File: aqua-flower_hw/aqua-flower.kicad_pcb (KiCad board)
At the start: 2 copper layers, 0 parts

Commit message: Place all pcb details and start to trace pcb.
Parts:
- added BZ1: BUZZER, Buzzers_Beepers:Buzzer_12x9.5RM7.6, F.Cu at (125.6, 93.8)
- added C1: 0.1u, Capacitors_SMD:C_0603_HandSoldering, F.Cu at (134.2, 99.0)
- added C10: 4u7, Capacitors_SMD:C_0603_HandSoldering, F.Cu at (180.8, 78.1)
- added C11: 0.1u, Capacitors_SMD:C_0603_HandSoldering, F.Cu at (184.7, 72.0)
- added C2: 4u7, Capacitors_SMD:C_0603_HandSoldering, F.Cu at (175.3, 92.2)
- added C3: 0.1u, Capacitors_SMD:C_0603_HandSoldering, F.Cu at (165.2, 100.3)
- added C4: 0.1u, Capacitors_SMD:C_0603_HandSoldering, F.Cu at (185.0, 77.9)
- added C5: 0.1u, Capacitors_SMD:C_0603_HandSoldering, F.Cu at (169.6, 94.4)
- added C6: 0.1u, Capacitors_SMD:C_0603_HandSoldering, F.Cu at (180.8, 84.0)
- added C7: 1u, Capacitors_SMD:C_0603_HandSoldering, F.Cu at (161.0, 100.3)
- added C8: 8p, Capacitors_SMD:C_0603_HandSoldering, F.Cu at (175.3, 86.3)
- added C9: 8p, Capacitors_SMD:C_0603_HandSoldering, F.Cu at (165.5, 94.4)
- added DA1: LD1117, TO_SOT_Packages_SMD:SOT-223, F.Cu at (150.6, 89.9)
- added DD1: STM32F100C8(B), Housings_QFP:LQFP-48_7x7mm_Pitch0.5mm, F.Cu at (144.7, 78.0)
- added Q1: NPN, TO_SOT_Packages_SMD:SOT-23_Handsoldering, F.Cu at (162.8, 70.3)
- added Q2: IRLML6302, TO_SOT_Packages_SMD:SOT-23_Handsoldering, F.Cu at (178.0, 62.1)
- added Q3: IRLML6302, TO_SOT_Packages_SMD:SOT-23_Handsoldering, F.Cu at (155.6, 75.9)
- added Q4: IRLML6302, TO_SOT_Packages_SMD:SOT-23_Handsoldering, F.Cu at (168.9, 70.3)
- added Q5: IRLML6302, TO_SOT_Packages_SMD:SOT-23_Handsoldering, F.Cu at (140.8, 98.2)
- added R1: 1k, Resistors_SMD:R_0603_HandSoldering, F.Cu at (156.7, 100.3)
- added R2: 10k, Resistors_SMD:R_0603_HandSoldering, F.Cu at (161.2, 94.4)
- added R3: 10k, Resistors_SMD:R_0603_HandSoldering, F.Cu at (156.7, 94.4)
- added R4: 10k, Resistors_SMD:R_0603_HandSoldering, F.Cu at (184.8, 66.1)
- added R5: 10k, Resistors_SMD:R_0603_HandSoldering, F.Cu at (184.5, 60.2)
- added SW1: BUTTON, Buttons_Switches_ThroughHole:SW_PUSH_SMALL, F.Cu at (177.9, 71.0)
- added SW2: BUTTON, Buttons_Switches_ThroughHole:SW_PUSH_SMALL, F.Cu at (168.5, 87.3)
- added SW3: BUTTON, Buttons_Switches_ThroughHole:SW_PUSH_SMALL, F.Cu at (174.0, 79.2)
- added SW4: BUTTON, Buttons_Switches_ThroughHole:SW_PUSH_SMALL, F.Cu at (149.8, 98.8)
- added SW5: BUTTON, Buttons_Switches_ThroughHole:SW_PUSH_SMALL, F.Cu at (159.1, 87.3)
- added SW6: BUTTON, Buttons_Switches_ThroughHole:SW_PUSH_SMALL, F.Cu at (164.6, 79.2)
- added XL1: CONN_5, Socket_Strips:Socket_Strip_Straight_1x05, F.Cu at (103.5, 99.1)
- added XL2: CONN_8, Socket_Strips:Socket_Strip_Straight_1x08, F.Cu at (103.5, 63.4)
- added XL3: CONN_3, Socket_Strips:Socket_Strip_Straight_1x03, F.Cu at (139.7, 91.2)
- added XL4: ST_SWD, Socket_Strips:Socket_Strip_Straight_1x04, F.Cu at (164.0, 63.4)
- added XL5: CONN_3, Connect:BARREL_JACK, F.Cu at (149.9, 64.3)
- added XL6: CONN_3, Connect:BARREL_JACK, F.Cu at (126.9, 78.0)
- added XL7: CONN_3, Connect:BARREL_JACK, F.Cu at (108.1, 86.2)
- added XL8: CONN_3, Connect:BARREL_JACK, F.Cu at (131.1, 64.3)
- added XL9: CONN_3, Connect:BARREL_JACK, F.Cu at (108.1, 72.5)
- added XTAL1: CRYSTAL, Crystals:Crystal_Watch, F.Cu at (134.3, 85.5)

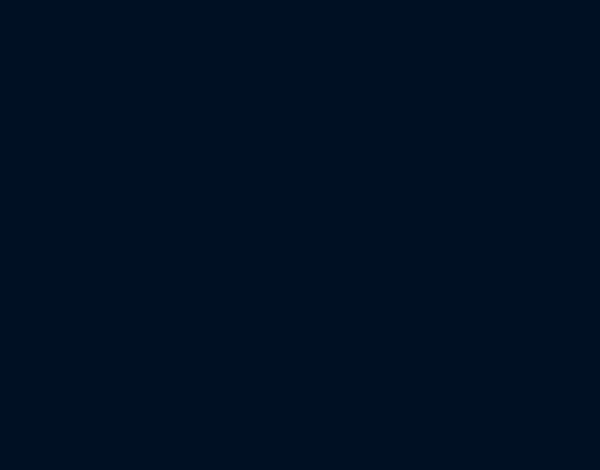
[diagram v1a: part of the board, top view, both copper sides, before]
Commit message: Reset Library Component
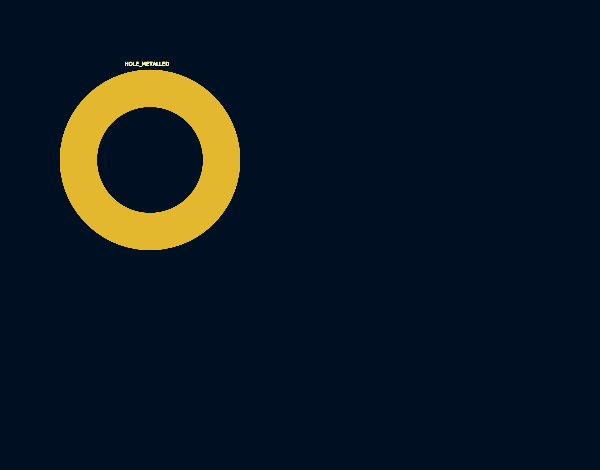
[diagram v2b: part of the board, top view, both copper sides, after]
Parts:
- added HOLE1, HOLE2, HOLE3, HOLE4: HOLE_METALLED, PCB:Hole3_5_out6mm, F.Cu at (0.00, 0.00)
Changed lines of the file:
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@@
 (kicad_pcb (version 4) (host pcbnew 4.0.2-stable)
   (general
-    (links 110)
-    (no_connects 110)
+    (links 114)
+    (no_connects 111)
     (area 0 0 0 0)
     (thickness 1.5)
@@
     (tracks 0)
     (zones 0)
-    (modules 40)
+    (modules 44)
     (nets 53)
   )
@@
       (net 52 "Net-(XL9-Pad3)"))
   )
+  (module PCB:Hole3_5_out6mm (layer F.Cu)
+    (at 0 0)
+    (fp_text reference HOLE1 (at 0 3.2004) (layer F.SilkS) hide
+      (effects (font (size 0.127 0.127) (thickness 0.00254)))
+    )
+    (fp_text value HOLE_METALLED (at -0.09906 -3.2004) (layer F.SilkS)
+      (effects (font (size 0.127 0.127) (thickness 0.00254)))
+    )
+    (pad H thru_hole circle (at 0 0) (size 6 6) (drill 3.5) (layers *.Cu *.Mask F.SilkS)
+      (net 2 GND))
+  )
+  (module PCB:Hole3_5_out6mm (layer F.Cu)
+    (at 0 0)
+    (fp_text reference HOLE2 (at 0 3.2004) (layer F.SilkS) hide
+      (effects (font (size 0.127 0.127) (thickness 0.00254)))
+    )
+    (fp_text value HOLE_METALLED (at -0.09906 -3.2004) (layer F.SilkS)
+      (effects (font (size 0.127 0.127) (thickness 0.00254)))
+    )
+    (pad H thru_hole circle (at 0 0) (size 6 6) (drill 3.5) (layers *.Cu *.Mask F.SilkS)
+      (net 2 GND))
+  )
+  (module PCB:Hole3_5_out6mm (layer F.Cu)
+    (at 0 0)
+    (fp_text reference HOLE3 (at 0 3.2004) (layer F.SilkS) hide
+      (effects (font (size 0.127 0.127) (thickness 0.00254)))
+    )
+    (fp_text value HOLE_METALLED (at -0.09906 -3.2004) (layer F.SilkS)
+      (effects (font (size 0.127 0.127) (thickness 0.00254)))
+    )
+    (pad H thru_hole circle (at 0 0) (size 6 6) (drill 3.5) (layers *.Cu *.Mask F.SilkS)
+      (net 2 GND))
+  )
+  (module PCB:Hole3_5_out6mm (layer F.Cu)
+    (at 0 0)
+    (fp_text reference HOLE4 (at 0 3.2004) (layer F.SilkS) hide
+      (effects (font (size 0.127 0.127) (thickness 0.00254)))
+    )
+    (fp_text value HOLE_METALLED (at -0.09906 -3.2004) (layer F.SilkS)
+      (effects (font (size 0.127 0.127) (thickness 0.00254)))
+    )
+    (pad H thru_hole circle (at 0 0) (size 6 6) (drill 3.5) (layers *.Cu *.Mask F.SilkS)
+      (net 2 GND))
+  )
 )

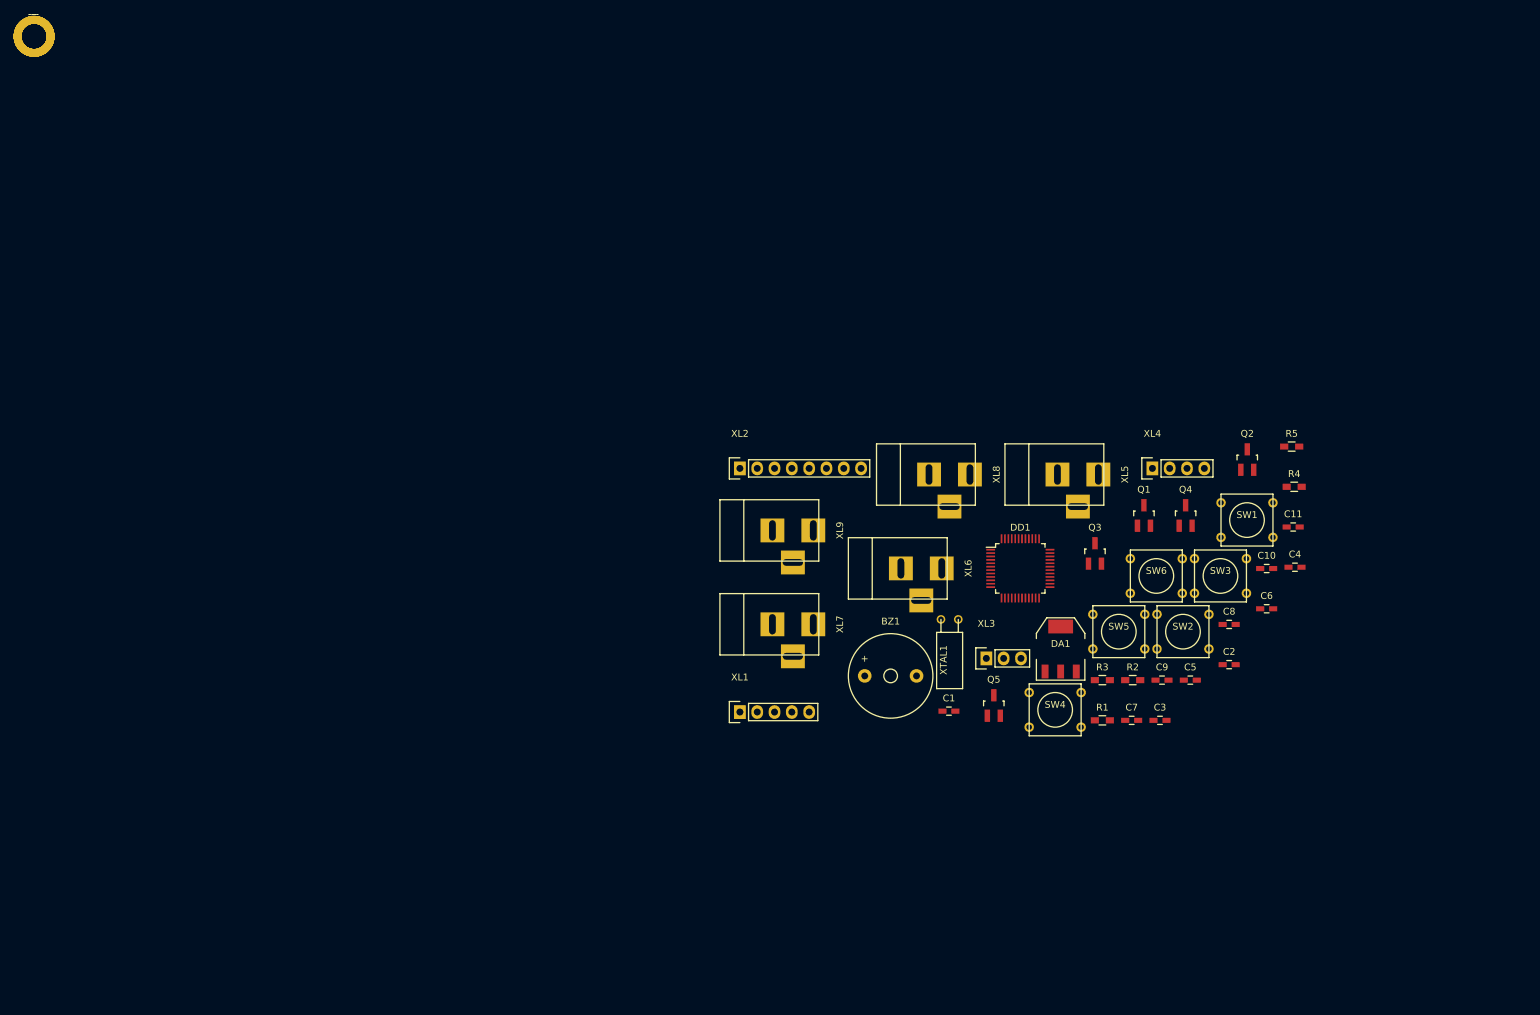
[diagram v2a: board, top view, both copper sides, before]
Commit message: Add holes
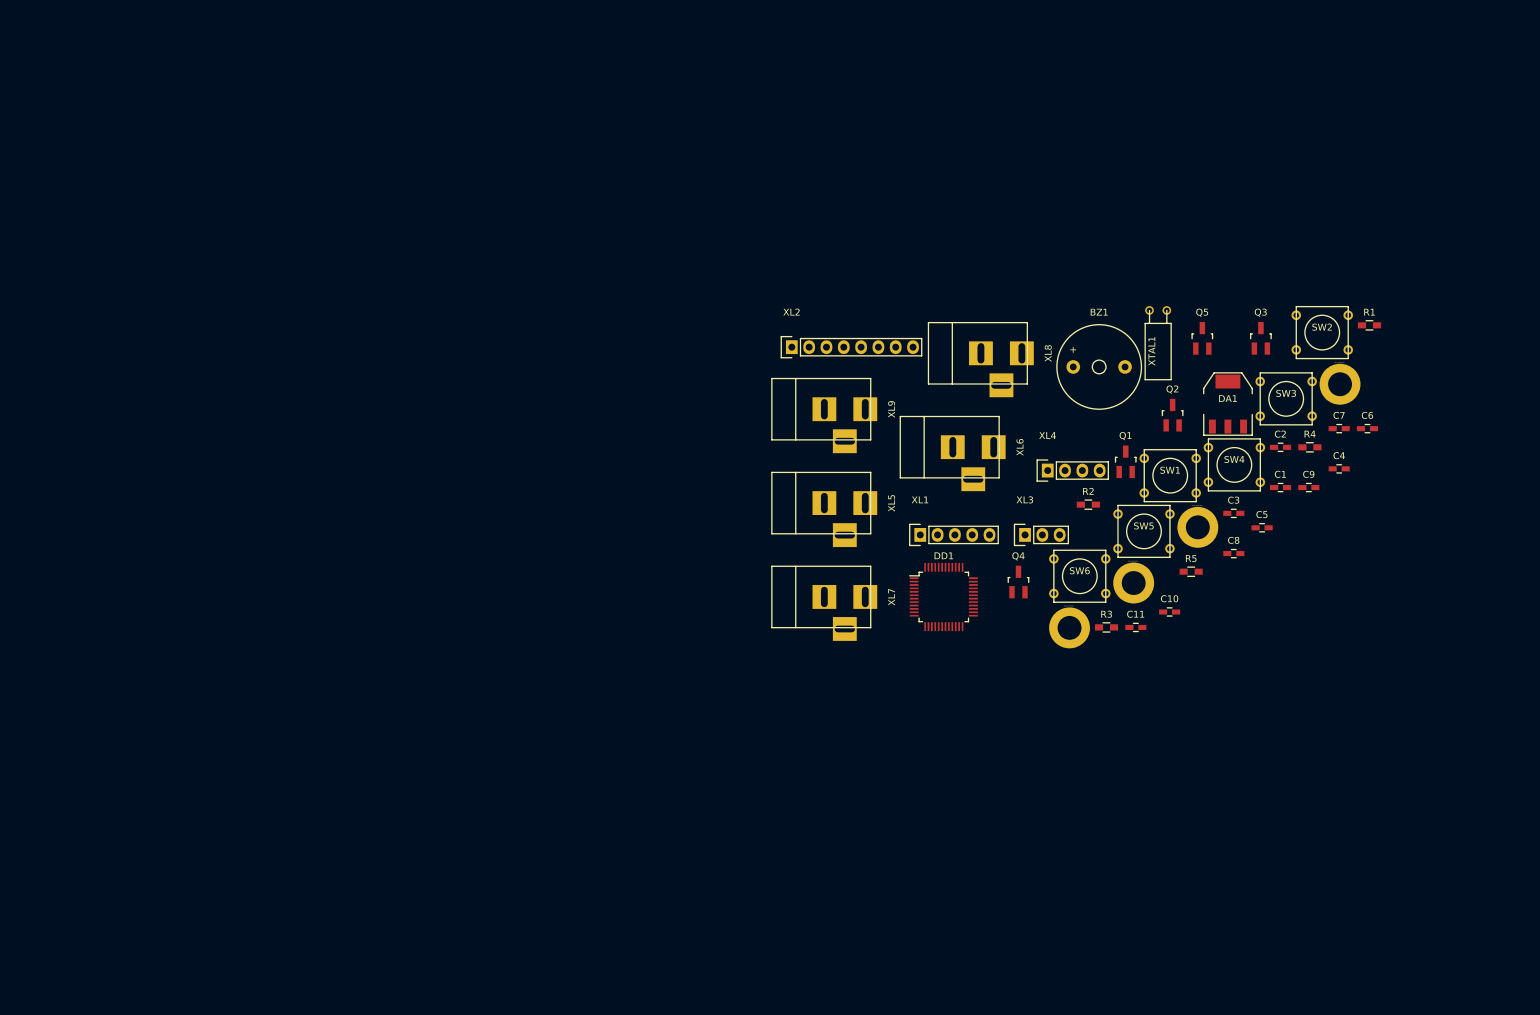
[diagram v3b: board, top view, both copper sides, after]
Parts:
- moved HOLE4 198.3 mm to (191.6, 51.0)
- moved HOLE2 185.3 mm to (170.7, 72.0)
- moved HOLE3 180.1 mm to (161.3, 80.2)
- moved HOLE1 174.9 mm to (151.9, 86.8)
- moved R1 69.9 mm to (195.9, 42.4)
- moved Q5 61.9 mm to (171.4, 44.3)
- moved C1 58.7 mm to (182.8, 66.2)
- moved XTAL1 54.7 mm to (164.9, 40.2)
- moved BZ1 54.7 mm to (156.2, 48.5)
- moved C7 52.5 mm to (191.4, 57.5)
- moved SW2 48.4 mm to (189.0, 43.5)
- moved SW4 44.5 mm to (176.1, 62.9)
- moved DA1 43.5 mm to (175.1, 53.9)
- moved Q3 39.8 mm to (180.0, 44.3)
- moved XL1 37.1 mm to (130.0, 73.1)
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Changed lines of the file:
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@@
   (general
     (links 114)
-    (no_connects 111)
+    (no_connects 114)
     (area 0 0 0 0)
     (thickness 1.5)
@@
   )
   (module Capacitors_SMD:C_0603_HandSoldering (layer F.Cu)
-    (at 134.195001 98.985)
+    (at 182.845001 66.185)
     (descr "Capacitor SMD 0603, hand soldering")
     (tags "capacitor 0603")
@@
   )
   (module Capacitors_SMD:C_0603_HandSoldering (layer F.Cu)
-    (at 175.305001 92.165)
+    (at 182.845001 60.285)
     (descr "Capacitor SMD 0603, hand soldering")
     (tags "capacitor 0603")
@@
   )
   (module Capacitors_SMD:C_0603_HandSoldering (layer F.Cu)
-    (at 165.155001 100.335)
+    (at 175.985001 69.975)
     (descr "Capacitor SMD 0603, hand soldering")
     (tags "capacitor 0603")
@@
   )
   (module Capacitors_SMD:C_0603_HandSoldering (layer F.Cu)
-    (at 184.955001 77.875)
+    (at 191.445001 63.445)
     (descr "Capacitor SMD 0603, hand soldering")
     (tags "capacitor 0603")
@@
   )
   (module Capacitors_SMD:C_0603_HandSoldering (layer F.Cu)
-    (at 169.605001 94.435)
+    (at 180.135001 72.085)
     (descr "Capacitor SMD 0603, hand soldering")
     (tags "capacitor 0603")
@@
   )
   (module Capacitors_SMD:C_0603_HandSoldering (layer F.Cu)
-    (at 180.805001 83.965)
+    (at 195.595001 57.545)
     (descr "Capacitor SMD 0603, hand soldering")
     (tags "capacitor 0603")
@@
   )
   (module Capacitors_SMD:C_0603_HandSoldering (layer F.Cu)
-    (at 161.005001 100.335)
+    (at 191.445001 57.545)
     (descr "Capacitor SMD 0603, hand soldering")
     (tags "capacitor 0603")
@@
   )
   (module Capacitors_SMD:C_0603_HandSoldering (layer F.Cu)
-    (at 175.305001 86.265)
+    (at 175.985001 75.875)
     (descr "Capacitor SMD 0603, hand soldering")
     (tags "capacitor 0603")
@@
   )
   (module Capacitors_SMD:C_0603_HandSoldering (layer F.Cu)
-    (at 165.455001 94.435)
+    (at 186.995001 66.185)
     (descr "Capacitor SMD 0603, hand soldering")
     (tags "capacitor 0603")
@@
   )
   (module Capacitors_SMD:C_0603_HandSoldering (layer F.Cu)
-    (at 180.805001 78.065)
+    (at 166.575001 84.435)
     (descr "Capacitor SMD 0603, hand soldering")
     (tags "capacitor 0603")
@@
   )
   (module Capacitors_SMD:C_0603_HandSoldering (layer F.Cu)
-    (at 184.695001 71.975)
+    (at 161.615001 86.705)
     (descr "Capacitor SMD 0603, hand soldering")
     (tags "capacitor 0603")
@@
   )
   (module Resistors_SMD:R_0603_HandSoldering (layer F.Cu)
-    (at 156.705001 100.335)
+    (at 195.885001 42.395)
     (descr "Resistor SMD 0603, hand soldering")
     (tags "resistor 0603")
@@
   )
   (module Resistors_SMD:R_0603_HandSoldering (layer F.Cu)
-    (at 161.155001 94.435)
+    (at 154.655001 68.695)
     (descr "Resistor SMD 0603, hand soldering")
     (tags "resistor 0603")
@@
   )
   (module Resistors_SMD:R_0603_HandSoldering (layer F.Cu)
-    (at 156.705001 94.435)
+    (at 157.315001 86.705)
     (descr "Resistor SMD 0603, hand soldering")
     (tags "resistor 0603")
@@
   )
   (module Resistors_SMD:R_0603_HandSoldering (layer F.Cu)
-    (at 184.845001 66.075)
+    (at 187.145001 60.285)
     (descr "Resistor SMD 0603, hand soldering")
     (tags "resistor 0603")
@@
   )
   (module Resistors_SMD:R_0603_HandSoldering (layer F.Cu)
-    (at 184.475001 60.175)
+    (at 169.735001 78.535)
     (descr "Resistor SMD 0603, hand soldering")
     (tags "resistor 0603")
@@
   )
   (module Buzzers_Beepers:Buzzer_12x9.5RM7.6 (layer F.Cu)
-    (at 125.645141 93.816)
+    (at 156.235141 48.496)
     (descr "Generic Buzzer, D12mm height 9.5mm with RM7.6mm")
     (tags buzzer)
@@
   )
   (module TO_SOT_Packages_SMD:SOT-223 (layer F.Cu)
-    (at 150.581001 89.867001)
+    (at 175.131001 53.937001)
     (descr "module CMS SOT223 4 pins")
     (tags "CMS SOT")
@@
   )
   (module Housings_QFP:LQFP-48_7x7mm_Pitch0.5mm (layer F.Cu)
-    (at 144.665953 78.045)
+    (at 133.445953 82.235)
     (descr "48 LEAD LQFP 7x7mm (see MICREL LQFP7x7-48LD-PL-1.pdf)")
     (tags "QFP 0.5")
@@
   )
   (module TO_SOT_Packages_SMD:SOT-23_Handsoldering (layer F.Cu)
-    (at 162.802619 70.285)
+    (at 160.132619 62.405)
     (descr "SOT-23, Handsoldering")
     (tags SOT-23)
@@
   )
   (module TO_SOT_Packages_SMD:SOT-23_Handsoldering (layer F.Cu)
-    (at 177.958809 62.085)
+    (at 167.008809 55.575)
     (descr "SOT-23, Handsoldering")
     (tags SOT-23)
@@
   )
   (module TO_SOT_Packages_SMD:SOT-23_Handsoldering (layer F.Cu)
-    (at 155.618809 75.855)
+    (at 179.958809 44.305)
     (descr "SOT-23, Handsoldering")
     (tags SOT-23)
@@
   )
   (module TO_SOT_Packages_SMD:SOT-23_Handsoldering (layer F.Cu)
-    (at 168.918809 70.285)
+    (at 144.398809 80.045)
     (descr "SOT-23, Handsoldering")
     (tags SOT-23)
@@
   )
   (module TO_SOT_Packages_SMD:SOT-23_Handsoldering (layer F.Cu)
-    (at 140.778809 98.155)
+    (at 171.368809 44.305)
     (descr "SOT-23, Handsoldering")
     (tags SOT-23)
@@
   )
   (module Buttons_Switches_ThroughHole:SW_PUSH_SMALL (layer F.Cu)
-    (at 177.9185 70.955001)
+    (at 166.6585 64.445001)
     (fp_text reference SW1 (at 0 -0.762) (layer F.SilkS)
       (effects (font (size 1 1) (thickness 0.15)))
@@
   )
   (module Buttons_Switches_ThroughHole:SW_PUSH_SMALL (layer F.Cu)
-    (at 168.5285 87.325001)
+    (at 188.9585 43.455001)
     (fp_text reference SW2 (at 0 -0.762) (layer F.SilkS)
       (effects (font (size 1 1) (thickness 0.15)))
@@
   )
   (module Buttons_Switches_ThroughHole:SW_PUSH_SMALL (layer F.Cu)
-    (at 174.0285 79.155001)
+    (at 183.6685 53.175001)
     (fp_text reference SW3 (at 0 -0.762) (layer F.SilkS)
       (effects (font (size 1 1) (thickness 0.15)))
@@
   )
   (module Buttons_Switches_ThroughHole:SW_PUSH_SMALL (layer F.Cu)
-    (at 149.7785 98.795001)
+    (at 176.0685 62.865001)
     (fp_text reference SW4 (at 0 -0.762) (layer F.SilkS)
       (effects (font (size 1 1) (thickness 0.15)))
@@
   )
   (module Buttons_Switches_ThroughHole:SW_PUSH_SMALL (layer F.Cu)
-    (at 159.1185 87.325001)
+    (at 162.8085 72.615001)
     (fp_text reference SW5 (at 0 -0.762) (layer F.SilkS)
       (effects (font (size 1 1) (thickness 0.15)))
@@
   )
   (module Buttons_Switches_ThroughHole:SW_PUSH_SMALL (layer F.Cu)
-    (at 164.6185 79.155001)
+    (at 153.3985 79.195001)
     (fp_text reference SW6 (at 0 -0.762) (layer F.SilkS)
       (effects (font (size 1 1) (thickness 0.15)))
@@
   )
   (module Socket_Strips:Socket_Strip_Straight_1x05 (layer F.Cu)
-    (at 103.533571 99.115)
+    (at 129.993571 73.135)
     (descr "Through hole socket strip")
     (tags "socket strip")
@@
   )
   (module Socket_Strips:Socket_Strip_Straight_1x08 (layer F.Cu)
-    (at 103.533571 63.375)
+    (at 111.153571 45.595)
     (descr "Through hole socket strip")
     (tags "socket strip")
@@
   )
   (module Socket_Strips:Socket_Strip_Straight_1x03 (layer F.Cu)
-    (at 139.683571 91.245)
+    (at 145.363571 73.135)
     (descr "Through hole socket strip")
     (tags "socket strip")
@@
   )
   (module Socket_Strips:Socket_Strip_Straight_1x04 (layer F.Cu)
-    (at 164.040714 63.375)
+    (at 148.690714 63.695)
     (descr "Through hole socket strip")
     (tags "socket strip")
@@
   )
   (module Crystals:Crystal_Watch (layer F.Cu)
-    (at 134.300001 85.525)
+    (at 164.890001 40.205)
     (fp_text reference XTAL1 (at -0.889 5.969 90) (layer F.SilkS)
       (effects (font (size 1 1) (thickness 0.15)))
@@
   )
   (module Connect:BARREL_JACK (layer F.Cu)
-    (at 149.915621 64.27448)
+    (at 115.725621 68.46448)
     (descr "DC Barrel Jack")
     (tags "Power Jack")
@@
   )
   (module Connect:BARREL_JACK (layer F.Cu)
-    (at 126.945621 78.04448)
+    (at 134.565621 60.26448)
     (descr "DC Barrel Jack")
     (tags "Power Jack")
@@
   )
   (module Connect:BARREL_JACK (layer F.Cu)
-    (at 108.105621 86.24448)
+    (at 115.725621 82.23448)
     (descr "DC Barrel Jack")
     (tags "Power Jack")
@@
   )
   (module Connect:BARREL_JACK (layer F.Cu)
-    (at 131.075621 64.27448)
+    (at 138.695621 46.49448)
     (descr "DC Barrel Jack")
     (tags "Power Jack")
@@
   )
   (module Connect:BARREL_JACK (layer F.Cu)
-    (at 108.105621 72.47448)
+    (at 115.725621 54.69448)
     (descr "DC Barrel Jack")
     (tags "Power Jack")
@@
   )
   (module PCB:Hole3_5_out6mm (layer F.Cu)
-    (at 0 0)
+    (at 151.89 86.77311)
     (fp_text reference HOLE1 (at 0 3.2004) (layer F.SilkS) hide
       (effects (font (size 0.127 0.127) (thickness 0.00254)))
@@
   )
   (module PCB:Hole3_5_out6mm (layer F.Cu)
-    (at 0 0)
+    (at 170.71 72.02311)
     (fp_text reference HOLE2 (at 0 3.2004) (layer F.SilkS) hide
       (effects (font (size 0.127 0.127) (thickness 0.00254)))
@@
   )
   (module PCB:Hole3_5_out6mm (layer F.Cu)
-    (at 0 0)
+    (at 161.3 80.19311)
     (fp_text reference HOLE3 (at 0 3.2004) (layer F.SilkS) hide
       (effects (font (size 0.127 0.127) (thickness 0.00254)))
@@
   )
   (module PCB:Hole3_5_out6mm (layer F.Cu)
-    (at 0 0)
+    (at 191.57 51.03311)
     (fp_text reference HOLE4 (at 0 3.2004) (layer F.SilkS) hide
       (effects (font (size 0.127 0.127) (thickness 0.00254)))
